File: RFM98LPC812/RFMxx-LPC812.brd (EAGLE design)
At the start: 60 x 40 mm, 21 parts, among them X1 BU-SMA-V, X2 BU-SMA-V

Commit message: no comment
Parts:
- moved U$4 33.2 mm to (48.3, 31.8), flipped to the bottom
- moved JP1 1.27 mm to (20.8, 31.8)
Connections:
- new net N$25: U$1.17, U$2.RESET, U$3.RESET
- net N$17: now also U$2.DIO4
- net N$18: now also U$2.DIO5
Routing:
- net N$25: track 0.00 -> 81.7 mm, vias 0 -> 4
- net GND: track 167.9 -> 235.0 mm
- net N$18: track 21.2 -> 63.5 mm, vias 0 -> 2
- net N$17: track 23.2 -> 47.1 mm, vias 0 -> 2
- net N$6: track 8.76 -> 0.00 mm
- net N$1: track 10.8 -> 6.03 mm
- net VCC: track 81.8 -> 78.0 mm
- net N$21: track 53.1 -> 51.2 mm, vias 1 -> 0
- net N$22: track 42.1 -> 40.3 mm
- net N$19: track 40.5 -> 39.6 mm
- removed copper zone on layer 1, net GND

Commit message: no comment
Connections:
- new net N$26: R1.1, R2.1, R3.1, R4.1, R5.1, R6.1, U$1.16, U$2.GND, U$2.GND2, U$2.GND3, U$3.GND, U$4.-, X2.2, X2.3, X2.4, X2.5
- net GND: no longer R1.1, R2.1, R3.1, R4.1, R5.1, R6.1, U$1.16, U$2.GND, U$3.GND, U$4.-, X2.2, X2.3, X2.4, X2.5
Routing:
- net N$26: track 0.00 -> 272.5 mm, vias 0 -> 5
- net GND: track 235.0 -> 15.5 mm, vias 3 -> 0
- net N$6: track 0.00 -> 7.00 mm

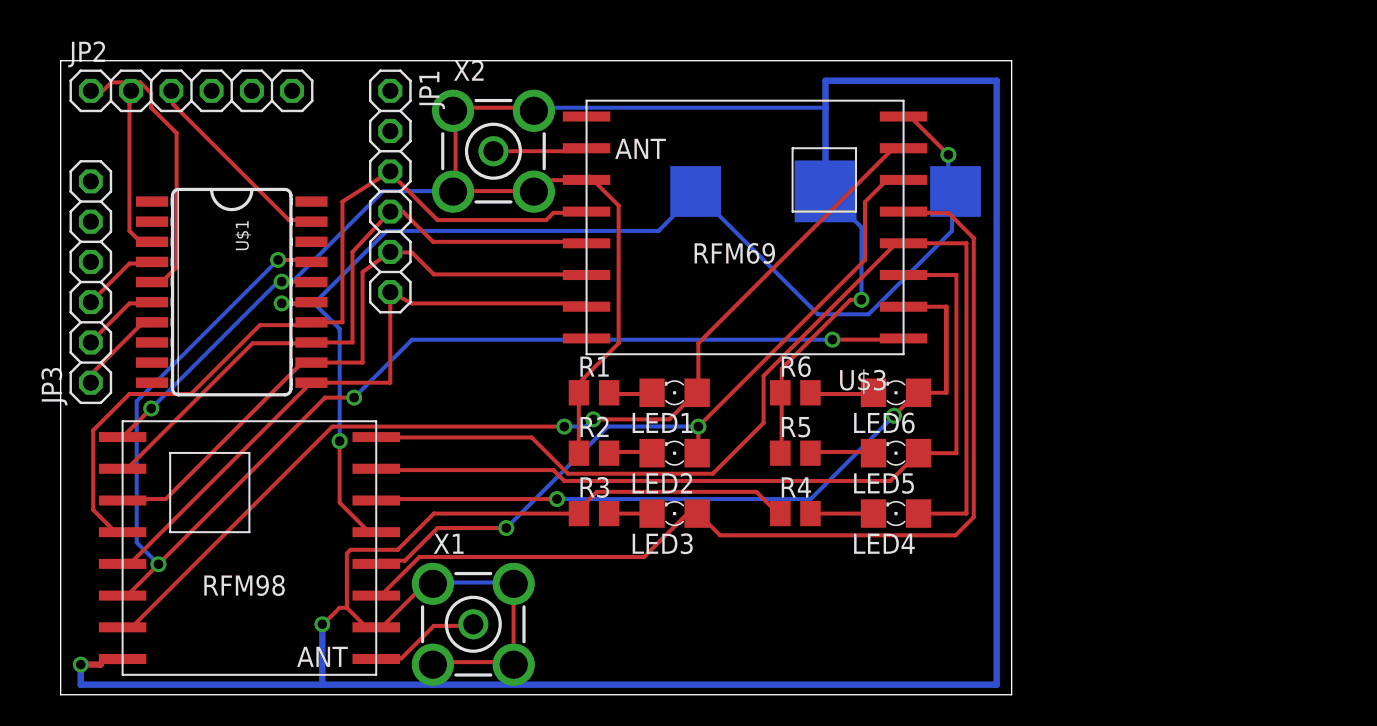
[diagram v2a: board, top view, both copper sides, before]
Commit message: reasonably good layout on RFM98 side
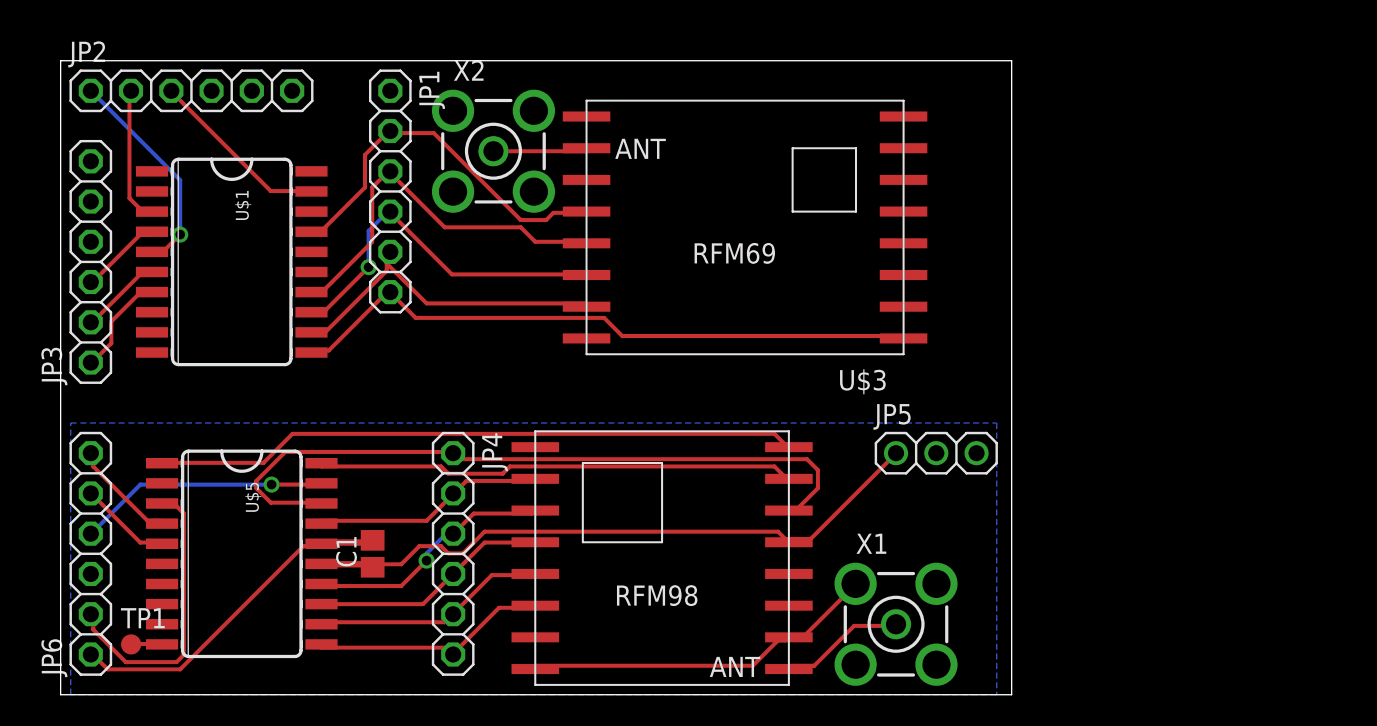
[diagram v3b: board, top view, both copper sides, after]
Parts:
- removed LED1, LED2, LED3, LED4, LED5, LED6: (no value), adafruit:1206
- removed R1, R2, R3, R4, R5, R6: (no value), resistor:M0805
- removed U$4: (no value), adafruit:CR1220-SMD
- added C1: 10uF, adafruit:C0805
- added JP4, JP6: (no value), adafruit:1X06
- added JP5: (no value), adafruit:1X03
- added TP1: TPB1,27, testpad:B1,27
- added U$5: LPC812M101JD20, LPC812:SOIC20
- moved X1 26.7 mm to (52.7, 4.45)
- moved U$2 26.0 mm to (37.9, 7.62)
- moved U$1 1.91 mm to (10.8, 26.0)
- moved JP3 1.27 mm to (1.91, 27.3)
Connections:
- removed net N$7: LED1.C, R1.2
- new net N$27: U$2.DIO1, U$5.20
- net GND: now also C1.2, JP5.2, JP6.1, U$2.GND2, U$2.GND3, U$5.16
- net N$10: now also JP4.4, U$2.SCK, U$5.13; no longer LED4.C, R4.2
- net N$11: now also JP4.2, U$2.MISO, U$5.17; no longer LED5.C, R5.2
- net N$12: now also JP4.6, U$2.RESET, U$5.11; no longer LED6.C, R6.2
- net N$13: now also JP1.6, U$1.11, U$3.RESET; no longer LED6.A, U$2.DIO0, U$3.DIO0
- net N$14: now also JP1.5, U$1.12, U$3.NSS; no longer LED5.A, U$2.DIO1, U$3.DIO1
- net N$15: now also JP1.4, U$1.13, U$3.MOSI; no longer LED4.A, U$2.DIO2, U$3.DIO2
- net N$16: now also JP1.3, U$1.14, U$3.MISO; no longer LED3.A, U$2.DIO3, U$3.DIO3
- net N$17: now also JP6.6, U$5.4; no longer LED2.A, U$2.DIO4, U$3.DIO4
- net N$18: now also JP6.5, U$5.5; no longer LED1.A, U$2.DIO5, U$3.DIO5
- net N$19: now also JP1.2, U$1.17, U$3.SCK; no longer JP1.5, U$1.12, U$2.MOSI, U$3.MOSI
- net N$20: now also JP6.4, U$5.19; no longer JP1.6, U$1.11, U$2.NSS, U$3.NSS
- net N$21: now also JP6.2, U$5.3; no longer JP1.3, U$1.14, U$2.SCK, U$3.SCK
- net N$22: now also JP4.1, U$2.DIO0, U$5.18; no longer JP1.4, U$1.13, U$2.MISO, U$3.MISO
- net N$25: now also TP1.TP, U$5.10; no longer U$1.17, U$2.RESET, U$3.RESET
- net N$26: now also U$2.DIO2, U$5.1; no longer R1.1, R2.1, R3.1, R4.1, R5.1, R6.1, U$1.16, U$2.GND, U$2.GND2, U$2.GND3, U$3.GND, U$4.-, X2.2, X2.3, X2.4, X2.5
- net N$8: now also JP4.5, U$2.NSS, U$5.12; no longer LED2.C, R2.2
- net N$9: now also JP4.3, U$2.MOSI, U$5.14; no longer LED3.C, R3.2
- net VCC: now also C1.1, JP5.1, U$5.15; no longer U$1.15, U$3.VCC, U$4.+$1, U$4.+$2
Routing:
- net N$26: track 272.5 -> 40.7 mm, vias 5 -> 0
- net N$25: track 81.7 -> 1.98 mm, vias 4 -> 0
- net N$18: track 63.5 -> 5.85 mm, vias 2 -> 0
- net N$15: track 66.0 -> 23.0 mm, vias 0 -> 1
- net N$17: track 47.1 -> 6.84 mm, vias 2 -> 0
- net N$16: track 63.7 -> 24.5 mm
- net VCC: track 78.0 -> 40.5 mm, vias 3 -> 0
- net N$21: track 51.2 -> 18.5 mm
- net N$27: track 0.00 -> 30.4 mm
- net N$14: track 52.2 -> 22.3 mm
- net GND: track 15.5 -> 44.5 mm
- net N$20: track 40.1 -> 15.9 mm, vias 0 -> 1
- net N$19: track 39.6 -> 23.8 mm
- net N$9: track 2.71 -> 15.8 mm, vias 0 -> 1
- net N$8: track 2.77 -> 14.9 mm
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- added copper zone on layer 16, net GND

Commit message: start working on RFM69
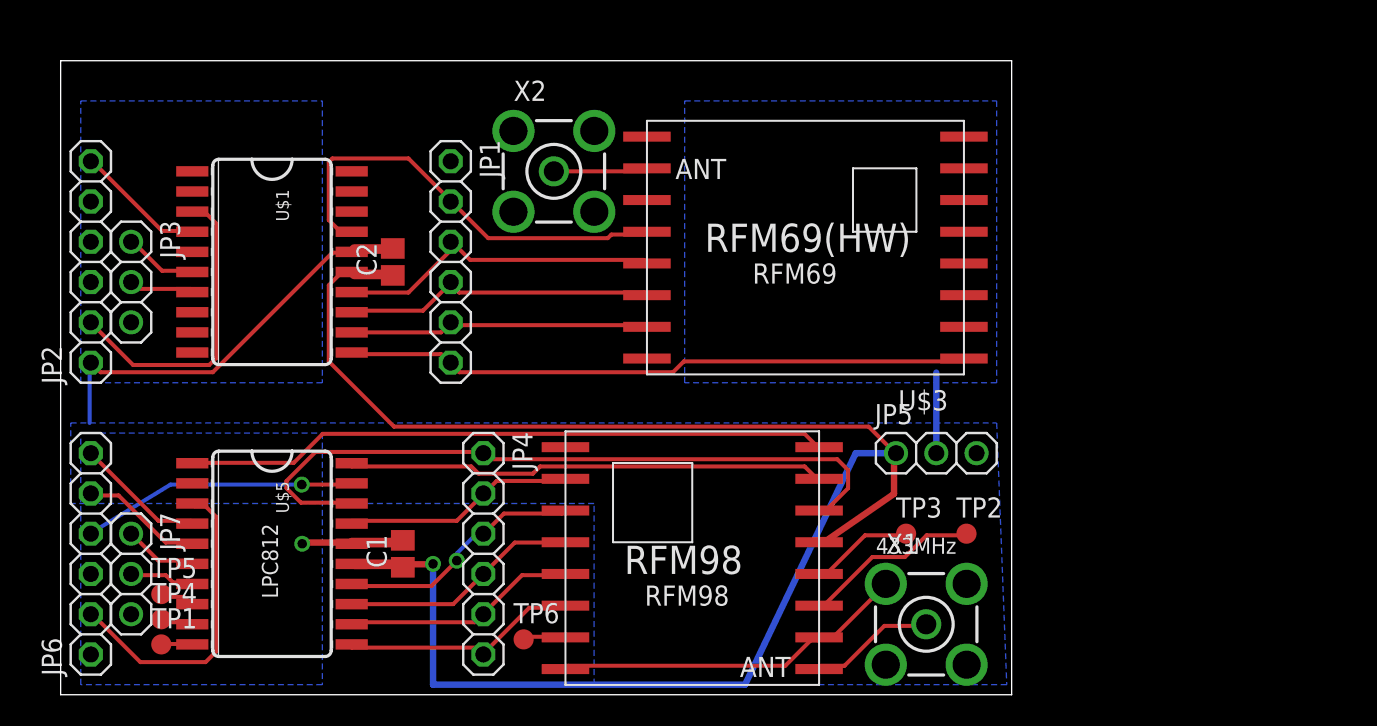
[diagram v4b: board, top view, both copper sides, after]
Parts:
- added C2: 0.1uF, adafruit:C0805
- added JP7: (no value), adafruit:1X03
- added TP2, TP3, TP4, TP5, TP6: TPB1,27, testpad:B1,27
- C1: value 10uF -> 0.1uF
- JP3: device adafruit:1X06 -> adafruit:1X03
- moved JP2 12.5 mm to (1.91, 27.3), turned to 90 degrees
- moved JP1 5.85 mm to (24.6, 27.3)
- moved U$3 4.02 mm to (47.0, 29.2)
- moved X2 4.02 mm to (31.1, 33.0)
- moved JP3 2.84 mm to (4.45, 26.0), turned to 270 degrees
- moved U$1 2.54 mm to (13.3, 26.0)
- moved C1 1.91 mm to (21.6, 8.89)
- moved JP4 1.91 mm to (26.7, 8.89)
- moved U$2 1.91 mm to (39.9, 7.62)
- moved U$5 1.91 mm to (13.3, 7.62)
- moved X1 1.91 mm to (54.6, 4.45)
- moved TP1 1.90 mm to (6.35, 3.17)
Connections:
- removed net N$2: JP3.1, U$1.7
- removed net N$24: JP2.3, U$1.19
- removed net N$4 (its old number): JP3.3, U$1.4
- new net N$23: JP3.2, U$1.7
- new net N$28: JP7.1, U$5.6
- new net N$29: JP7.2, U$5.7
- new net N$30: TP2.TP, U$2.DIO3
- new net N$31: TP3.TP, U$2.DIO4
- new net N$32: TP4.TP, U$5.9
- new net N$33: TP5.TP, U$5.8
- new net N$34: TP6.TP, U$2.DIO5
- net GND: now also C2.2, JP2.1, U$1.16
- net N$3: now also JP3.1; no longer JP3.2
- net N$5: now also JP2.6, U$1.4; no longer JP2.1, U$1.5
- net VCC: now also C2.1, U$1.15
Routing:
- net VCC: track 40.5 -> 107.2 mm, vias 0 -> 1
- net GND: track 44.5 -> 61.1 mm, vias 0 -> 1
- net N$24: track 11.5 -> 0.00 mm
- net N$30: track 0.00 -> 11.3 mm
- net N$4: track 8.63 -> 19.5 mm
- net N$31: track 0.00 -> 6.55 mm
- net N$2: track 6.49 -> 0.00 mm
- net N$5: track 13.6 -> 8.22 mm, vias 1 -> 0
- net N$4 (its old number): track 5.23 -> 0.00 mm
- net N$28: track 0.00 -> 4.70 mm
- net N$23: track 0.00 -> 4.21 mm
- net N$29: track 0.00 -> 4.12 mm
- net N$19: track 23.8 -> 27.8 mm
- net N$16: track 24.5 -> 21.1 mm
- net N$14: track 22.3 -> 19.0 mm
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- added copper zone on layer 16, net N$2
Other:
- board text added: "433MHz"
- board text added: "LPC812"
- board text added: "RFM69(HW)"
- board text added: "RFM98"

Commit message: start removing ground plane on RFM98 side
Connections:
- net GND: now also X2.2, X2.3, X2.4, X2.5
- net VCC: now also U$3.VCC
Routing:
- net GND: track 61.1 -> 218.1 mm
- net VCC: track 107.2 -> 132.7 mm
- net N$9: track 15.8 -> 15.7 mm, vias 1 -> 0
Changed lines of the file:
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@@
 <setting verticaltext="up"/>
 </settings>
-<grid distance="0.025" unitdist="inch" unit="inch" style="lines" multiple="1" display="yes" altdistance="0.025" altunitdist="inch" altunit="inch"/>
+<grid distance="0.0125" unitdist="inch" unit="inch" style="lines" multiple="1" display="yes" altdistance="0.025" altunitdist="inch" altunit="inch"/>
 <layers>
 <layer number="1" name="Top" color="4" fill="1" visible="yes" active="yes"/>
@@
 <contactref element="U$5" pad="15"/>
 <wire x1="52.705" y1="15.24" x2="50.165" y2="15.24" width="0.4064" layer="16"/>
-<wire x1="50.165" y1="15.24" x2="43.18" y2="0.635" width="0.4064" layer="16"/>
-<wire x1="43.18" y1="0.635" x2="23.495" y2="0.635" width="0.4064" layer="16"/>
-<wire x1="23.495" y1="0.635" x2="23.495" y2="8.255" width="0.4064" layer="16"/>
+<wire x1="50.165" y1="15.24" x2="28.8925" y2="8.89" width="0.4064" layer="16"/>
+<wire x1="28.8925" y1="8.89" x2="24.765" y2="8.89" width="0.4064" layer="16"/>
+<wire x1="24.765" y1="8.89" x2="23.495" y2="8.255" width="0.4064" layer="16"/>
 <via x="23.495" y="8.255" extent="1-16" drill="0.6"/>
 <wire x1="23.3172" y1="8.2296" x2="21.717" y2="8.2296" width="0.4064" layer="1"/>
@@
 <wire x1="20.8026" y1="26.5176" x2="20.955" y2="26.455" width="0.254" layer="1"/>
 <wire x1="18.5166" y1="26.5176" x2="18.3642" y2="26.67" width="0.254" layer="1"/>
+<contactref element="U$3" pad="VCC"/>
+<wire x1="45.4914" y1="35.2044" x2="56.9214" y2="35.2044" width="0.254" layer="1"/>
+<wire x1="38.6334" y1="28.3464" x2="45.4914" y2="35.2044" width="0.254" layer="1"/>
+<wire x1="26.5176" y1="28.3464" x2="38.6334" y2="28.3464" width="0.254" layer="1"/>
+<wire x1="25.146" y1="29.718" x2="26.5176" y2="28.3464" width="0.254" layer="1"/>
+<wire x1="24.003" y1="29.718" x2="25.146" y2="29.718" width="0.254" layer="1"/>
+<wire x1="22.1742" y1="27.8892" x2="24.003" y2="29.718" width="0.254" layer="1"/>
+<wire x1="22.1742" y1="27.432" x2="22.1742" y2="27.8892" width="0.254" layer="1"/>
+<wire x1="21.0312" y1="26.289" x2="22.1742" y2="27.432" width="0.254" layer="1"/>
+<wire x1="56.9214" y1="35.2044" x2="56.99" y2="35.21" width="0.254" layer="1"/>
+<wire x1="21.0312" y1="26.289" x2="20.955" y2="26.455" width="0.254" layer="1"/>
 </signal>
 <signal name="N$6">
@@
 <contactref element="JP4" pad="3"/>
 <contactref element="U$2" pad="MOSI"/>
-<wire x1="23.3934" y1="6.858" x2="18.3642" y2="6.858" width="0.254" layer="1"/>
-<wire x1="24.9936" y1="8.4582" x2="23.3934" y2="6.858" width="0.254" layer="1"/>
-<wire x1="24.9936" y1="8.9154" x2="24.9936" y2="8.4582" width="0.254" layer="16"/>
-<wire x1="26.1366" y1="10.0584" x2="24.9936" y2="8.9154" width="0.254" layer="16"/>
-<wire x1="26.5938" y1="10.0584" x2="26.1366" y2="10.0584" width="0.254" layer="16"/>
-<wire x1="18.3642" y1="6.858" x2="18.3642" y2="6.985" width="0.254" layer="1"/>
-<wire x1="26.5938" y1="10.0584" x2="26.67" y2="10.16" width="0.254" layer="16"/>
-<wire x1="27.9654" y1="11.43" x2="31.623" y2="11.43" width="0.254" layer="1"/>
-<wire x1="26.8224" y1="10.287" x2="27.9654" y2="11.43" width="0.254" layer="1"/>
+<wire x1="27.8892" y1="11.43" x2="31.623" y2="11.43" width="0.254" layer="1"/>
 <wire x1="31.623" y1="11.43" x2="31.85" y2="11.62" width="0.254" layer="1"/>
 <wire x1="26.8224" y1="10.287" x2="26.67" y2="10.16" width="0.254" layer="1"/>
-<via x="24.9936" y="8.4582" extent="1-16" drill="0.6096"/>
+<wire x1="23.3172" y1="6.858" x2="18.5166" y2="6.858" width="0.254" layer="1"/>
+<wire x1="26.5176" y1="10.0584" x2="23.3172" y2="6.858" width="0.254" layer="1"/>
+<wire x1="18.5166" y1="6.858" x2="18.3642" y2="6.985" width="0.254" layer="1"/>
+<wire x1="26.5176" y1="10.0584" x2="26.67" y2="10.16" width="0.254" layer="1"/>
+<wire x1="26.7462" y1="10.287" x2="27.8892" y2="11.43" width="0.254" layer="1"/>
+<wire x1="26.7462" y1="10.287" x2="26.67" y2="10.16" width="0.254" layer="1"/>
 </signal>
 <signal name="N$10">
@@
 <wire x1="32.004" y1="1.8288" x2="31.85" y2="1.62" width="0.254" layer="1"/>
 <wire x1="47.7774" y1="3.429" x2="47.85" y2="3.62" width="0.254" layer="1"/>
-<polygon width="0.4064" layer="16">
-<vertex x="0.635" y="17.145"/>
-<vertex x="59.055" y="17.145"/>
-<vertex x="59.69" y="0.635"/>
-<vertex x="33.655" y="0.635"/>
-<vertex x="33.655" y="12.065"/>
-<vertex x="0.635" y="12.065"/>
-</polygon>
-<polygon width="0.4064" layer="16">
-<vertex x="1.27" y="16.51"/>
-<vertex x="16.51" y="16.51"/>
-<vertex x="16.51" y="0.635"/>
-<vertex x="1.27" y="0.635"/>
-</polygon>
-<wire x1="18.3642" y1="9.6012" x2="15.3162" y2="9.6012" width="0.4064" layer="1"/>
+<wire x1="18.3642" y1="9.6012" x2="15.3162" y2="9.6012" width="0.6096" layer="1"/>
 <wire x1="15.3162" y1="9.6012" x2="15.24" y2="9.525" width="0.4064" layer="1"/>
 <wire x1="15.3162" y1="9.3726" x2="15.24" y2="9.525" width="0.254" layer="1"/>
@@
 </polygon>
 <wire x1="55.245" y1="15.24" x2="55.245" y2="20.32" width="0.4064" layer="16"/>
-<wire x1="1.8288" y1="17.145" x2="1.8288" y2="20.8026" width="0.254" layer="16"/>
+<wire x1="1.8288" y1="17.145" x2="1.8288" y2="18.9738" width="0.254" layer="16"/>
+<wire x1="1.8288" y1="18.9738" x2="1.8288" y2="20.8026" width="0.254" layer="16"/>
 <wire x1="1.8288" y1="20.8026" x2="1.905" y2="20.955" width="0.254" layer="16"/>
 <wire x1="17.145" y1="27.8892" x2="18.288" y2="27.8892" width="0.254" layer="1"/>
@@
 <wire x1="20.8026" y1="28.1178" x2="20.955" y2="28.155" width="0.254" layer="1"/>
 <wire x1="18.5166" y1="28.1178" x2="18.3642" y2="27.94" width="0.254" layer="1"/>
+<contactref element="X2" pad="2"/>
+<contactref element="X2" pad="3"/>
+<contactref element="X2" pad="4"/>
+<contactref element="X2" pad="5"/>
+<wire x1="28.575" y1="35.433" x2="28.575" y2="30.6324" width="0.254" layer="1"/>
+<wire x1="28.575" y1="35.433" x2="28.5676" y2="35.5699" width="0.254" layer="1"/>
+<wire x1="33.8328" y1="35.433" x2="33.8328" y2="30.6324" width="0.254" layer="16"/>
+<wire x1="33.8328" y1="35.433" x2="33.6674" y2="35.5699" width="0.254" layer="16"/>
+<wire x1="33.6042" y1="30.6324" x2="28.575" y2="30.6324" width="0.254" layer="1"/>
+<wire x1="28.575" y1="30.6324" x2="28.5676" y2="30.4701" width="0.254" layer="1"/>
+<wire x1="33.6042" y1="30.6324" x2="33.6674" y2="30.4701" width="0.254" layer="1"/>
+<wire x1="39.37" y1="30.6324" x2="33.8328" y2="30.6324" width="0.254" layer="16"/>
+<wire x1="33.8328" y1="30.6324" x2="33.6674" y2="30.4701" width="0.254" layer="16"/>
+<wire x1="55.245" y1="15.24" x2="55.245" y2="6.985" width="0.6096" layer="16"/>
+<wire x1="55.245" y1="6.985" x2="57.15" y2="6.985" width="0.4064" layer="16"/>
+<wire x1="57.15" y1="6.985" x2="57.15" y2="1.905" width="0.4064" layer="16"/>
+<wire x1="57.15" y1="1.905" x2="52.07" y2="1.905" width="0.4064" layer="16"/>
+<wire x1="52.07" y1="1.905" x2="52.07" y2="6.985" width="0.4064" layer="16"/>
+<wire x1="52.07" y1="6.985" x2="55.245" y2="6.985" width="0.4064" layer="16"/>
+<wire x1="52.07" y1="1.905" x2="15.24" y2="1.905" width="0.6096" layer="16"/>
+<wire x1="15.24" y1="1.905" x2="1.905" y2="1.905" width="0.6096" layer="16"/>
+<wire x1="1.905" y1="1.905" x2="1.905" y2="2.54" width="0.4064" layer="16"/>
+<wire x1="15.24" y1="9.525" x2="15.24" y2="1.905" width="0.6096" layer="16"/>
+<wire x1="52.1208" y1="2.0574" x2="52.0601" y2="1.8951" width="0.254" layer="16"/>
+<wire x1="52.1208" y1="2.0574" x2="52.07" y2="1.905" width="0.254" layer="16"/>
+<wire x1="57.15" y1="2.0574" x2="52.1208" y2="2.0574" width="0.254" layer="1"/>
+<wire x1="52.1208" y1="2.0574" x2="52.0601" y2="1.8951" width="0.254" layer="1"/>
+<wire x1="57.15" y1="2.0574" x2="57.1599" y2="1.8951" width="0.254" layer="1"/>
+<wire x1="57.15" y1="7.0866" x2="57.1599" y2="6.9949" width="0.254" layer="16"/>
+<wire x1="57.15" y1="7.0866" x2="57.15" y2="6.985" width="0.254" layer="16"/>
+<wire x1="52.1208" y1="7.0866" x2="57.15" y2="7.0866" width="0.254" layer="1"/>
+<wire x1="57.15" y1="7.0866" x2="57.1599" y2="6.9949" width="0.254" layer="1"/>
+<wire x1="52.1208" y1="7.0866" x2="52.0601" y2="6.9949" width="0.254" layer="1"/>
+<wire x1="17.3736" y1="19.6596" x2="39.3192" y2="19.6596" width="0.254" layer="16"/>
+<wire x1="16.6878" y1="18.9738" x2="17.3736" y2="19.6596" width="0.254" layer="16"/>
+<wire x1="1.8288" y1="18.9738" x2="16.6878" y2="18.9738" width="0.254" layer="16"/>
+<wire x1="39.3192" y1="19.6596" x2="39.37" y2="19.685" width="0.254" layer="16"/>
 </signal>
 <signal name="N$11">
